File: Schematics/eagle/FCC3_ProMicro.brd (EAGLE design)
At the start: 42.9 x 36 mm, 9 parts, among them IC1 MCP3202P

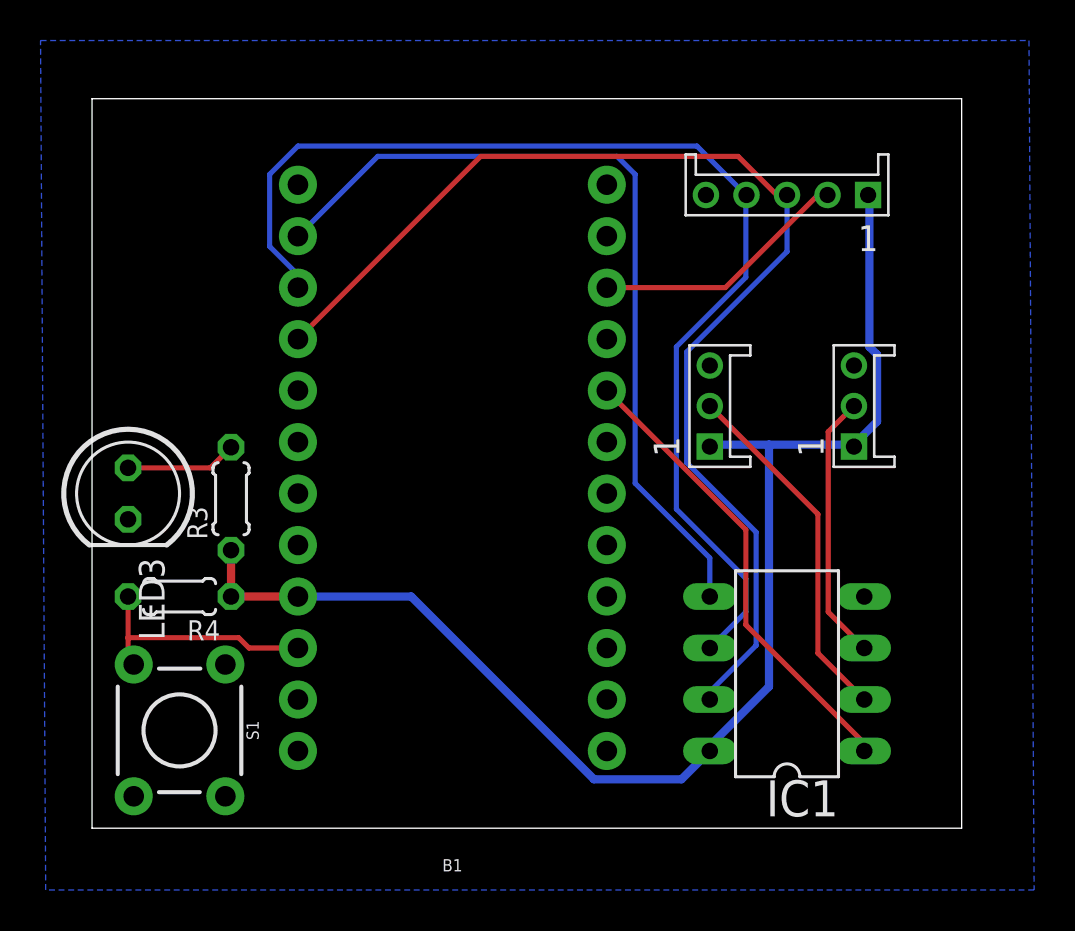
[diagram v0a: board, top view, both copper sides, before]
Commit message: replace force mapping with Analog/Digital FLCS
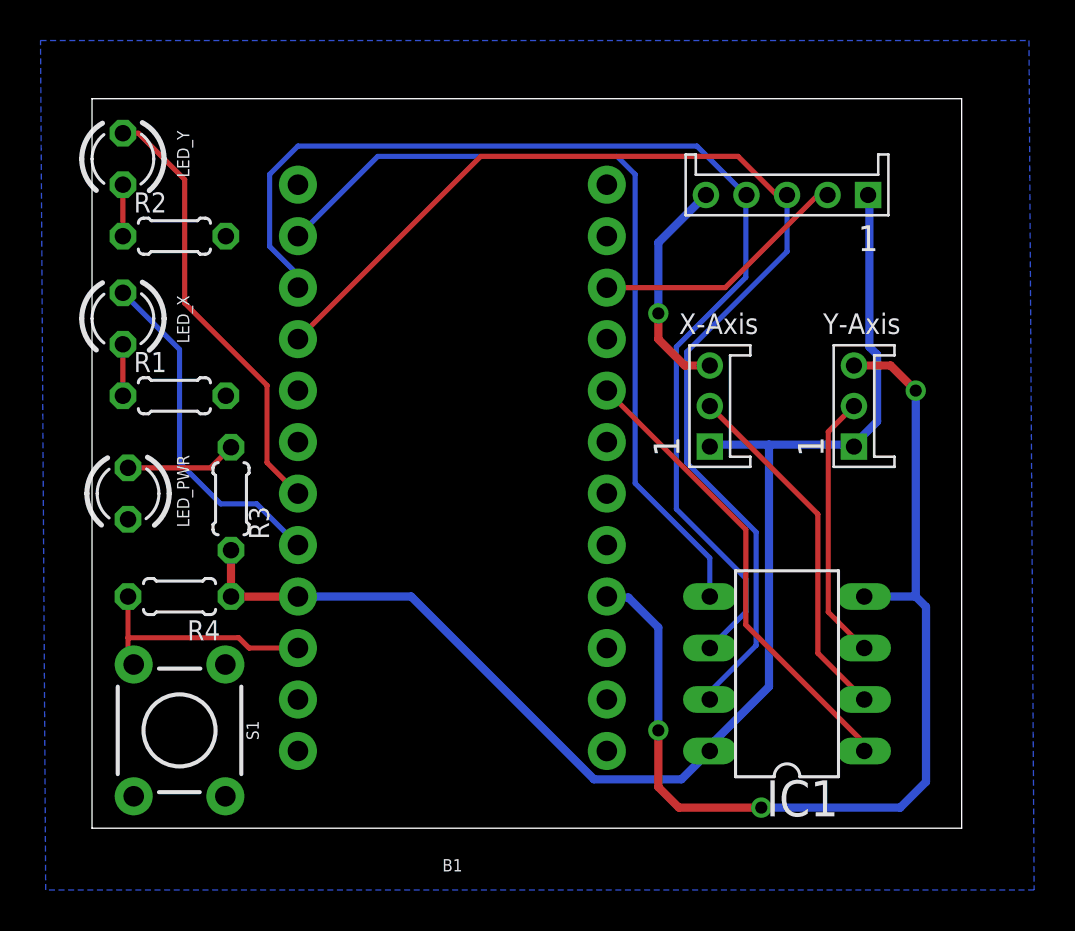
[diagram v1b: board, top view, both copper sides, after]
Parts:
- removed LED3: (no value), led:LED5MM
- added LED_PWR, LED_X, LED_Y: (no value), led:LED3MM
- added R1, R2: (no value), resistor:0204/5
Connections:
- new net N$3: B1.20, LED_X.A
- new net N$4: B1.19, LED_Y.A
- new net N$6: LED_Y.K, R2.1
- new net N$7: LED_X.K, R1.1
- net GND: now also LED_PWR.K, R1.2, R2.2; no longer LED3.K
- net N$5: now also LED_PWR.A; no longer LED3.A
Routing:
- net GND: track 0.00 -> 62.1 mm, vias 0 -> 4
- net N$4: track 0.00 -> 21.8 mm
- net N$3: track 0.00 -> 17.1 mm
- net N$7: track 0.00 -> 2.54 mm
- net N$6: track 0.00 -> 2.54 mm
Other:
- board text added: "X-Axis"
- board text added: "Y-Axis"
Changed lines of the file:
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@@
 <wire x1="42.906" y1="35.992" x2="0" y2="35.992" width="0" layer="20"/>
 <wire x1="0" y1="35.992" x2="0" y2="0" width="0" layer="20"/>
+<text x="28.956" y="24.384" size="1.016" layer="25">X-Axis</text>
+<text x="36.068" y="24.384" size="1.016" layer="25">Y-Axis</text>
 </plain>
 <attributes>
@@
 <attribute name="OC_FARNELL" value="1196794" x="34.29" y="7.62" size="1.778" layer="27" rot="R90" display="off"/>
 </element>
-<element name="LED3" library="led" package="LED5MM" value="" x="1.778" y="16.51" rot="R270"/>
-<element name="R3" library="resistor" package="0204/5" value="" x="6.858" y="16.256" rot="R90"/>
+<element name="LED_PWR" library="led" package="LED3MM" value="" x="1.778" y="16.51" smashed="yes" rot="R270">
+<attribute name="NAME" x="4.191" y="18.415" size="0.6096" layer="25" ratio="10" rot="R270"/>
+<attribute name="VALUE" x="0.127" y="14.605" size="1.27" layer="27" ratio="10" rot="R270"/>
+</element>
+<element name="R3" library="resistor" package="0204/5" value="" x="6.858" y="16.256" smashed="yes" rot="R90">
+<attribute name="NAME" x="8.7376" y="14.2494" size="0.9906" layer="25" ratio="10" rot="R90"/>
+<attribute name="VALUE" x="9.1694" y="14.1224" size="0.9906" layer="27" ratio="10" rot="R90"/>
+</element>
 <element name="R4" library="resistor" package="0204/5" value="" x="4.318" y="11.43" rot="R180"/>
 <element name="S1" library="SparkFun-Switches" package="TACTILE_SWITCH_PTH_6.0MM" value="MOMENTARY-SWITCH-SPST-PTH-6.0MM" x="4.318" y="4.826" rot="R270">
@@
 <element name="U$2" library="uriba" package="JST-EH-3PIN" value="JST_EH_3PIN" x="30.48" y="20.828" rot="R270"/>
 <element name="U$3" library="uriba" package="JST-EH-5PIN" value="JST_EH_5PIN" x="34.29" y="31.242"/>
+<element name="LED_X" library="led" package="LED3MM" value="" x="1.524" y="25.146" smashed="yes" rot="R270">
+<attribute name="NAME" x="4.191" y="26.289" size="0.6096" layer="25" ratio="10" rot="R270"/>
+<attribute name="VALUE" x="-0.127" y="23.241" size="1.27" layer="27" ratio="10" rot="R270"/>
+</element>
+<element name="LED_Y" library="led" package="LED3MM" value="" x="1.524" y="33.02" smashed="yes" rot="R270">
+<attribute name="NAME" x="4.191" y="34.417" size="0.6096" layer="25" ratio="10" rot="R270"/>
+<attribute name="VALUE" x="-0.127" y="31.115" size="1.27" layer="27" ratio="10" rot="R270"/>
+</element>
+<element name="R1" library="resistor" package="0204/5" value="" x="4.064" y="21.336"/>
+<element name="R2" library="resistor" package="0204/5" value="" x="4.064" y="29.21"/>
 </elements>
 <signals>
@@
 <contactref element="B1" pad="23"/>
 <contactref element="B1" pad="3"/>
-<contactref element="LED3" pad="K"/>
+<contactref element="LED_PWR" pad="K"/>
 <contactref element="S1" pad="1"/>
 <contactref element="B1" pad="4"/>
@@
 <vertex x="-2.286" y="-3.048"/>
 </polygon>
-<wire x1="37.592" y1="22.828" x2="38.1" y2="11.43" width="0" layer="19" extent="1-1"/>
-<wire x1="30.29" y1="31.242" x2="30.48" y2="22.828" width="0" layer="19" extent="1-1"/>
-<wire x1="25.4" y1="11.43" x2="30.48" y2="22.828" width="0" layer="19" extent="1-1"/>
+<contactref element="R1" pad="2"/>
+<contactref element="R2" pad="2"/>
+<wire x1="25.4" y1="9.017" x2="25.4" y2="8.89" width="0.4064" layer="16"/>
+<wire x1="37.592" y1="22.828" x2="39.402" y2="22.828" width="0.4064" layer="1"/>
+<wire x1="39.402" y1="22.828" x2="40.64" y2="21.59" width="0.4064" layer="1"/>
+<via x="40.64" y="21.59" extent="1-16" drill="0.6" shape="square"/>
+<wire x1="40.64" y1="21.59" x2="40.64" y2="11.43" width="0.4064" layer="16"/>
+<wire x1="40.64" y1="11.43" x2="38.1" y2="11.43" width="0.4064" layer="16"/>
+<wire x1="30.48" y1="22.828" x2="29.242" y2="22.828" width="0.4064" layer="1"/>
+<wire x1="29.242" y1="22.828" x2="27.94" y2="24.13" width="0.4064" layer="1"/>
+<wire x1="27.94" y1="24.13" x2="27.94" y2="25.4" width="0.4064" layer="1"/>
+<via x="27.94" y="25.4" extent="1-16" drill="0.6" shape="square"/>
+<wire x1="27.94" y1="25.4" x2="27.94" y2="28.892" width="0.4064" layer="16"/>
+<wire x1="27.94" y1="28.892" x2="30.29" y2="31.242" width="0.4064" layer="16"/>
+<wire x1="25.34919375" y1="11.379178125" x2="26.466821875" y2="11.379178125" width="0.4064" layer="16"/>
+<wire x1="26.466821875" y1="11.379178125" x2="27.94" y2="9.906" width="0.4064" layer="16"/>
+<wire x1="27.94" y1="9.906" x2="27.94" y2="4.826" width="0.4064" layer="16"/>
+<via x="27.94" y="4.826" extent="1-16" drill="0.6" shape="square"/>
+<wire x1="27.94" y1="4.826" x2="27.94" y2="2.032" width="0.4064" layer="1"/>
+<wire x1="27.94" y1="2.032" x2="28.956" y2="1.016" width="0.4064" layer="1"/>
+<wire x1="28.956" y1="1.016" x2="33.02" y2="1.016" width="0.4064" layer="1"/>
+<via x="33.02" y="1.016" extent="1-16" drill="0.6" shape="square"/>
+<wire x1="33.02" y1="1.016" x2="39.878" y2="1.016" width="0.4064" layer="16"/>
+<wire x1="39.878" y1="1.016" x2="41.148" y2="2.286" width="0.4064" layer="16"/>
+<wire x1="41.148" y1="2.286" x2="41.148" y2="10.922" width="0.4064" layer="16"/>
+<wire x1="41.148" y1="10.922" x2="40.64" y2="11.43" width="0.4064" layer="16"/>
 </signal>
 <signal name="RAW">
@@
 </signal>
 <signal name="N$5">
-<contactref element="LED3" pad="A"/>
+<contactref element="LED_PWR" pad="A"/>
 <contactref element="R3" pad="2"/>
 <wire x1="5.842" y1="17.78" x2="1.778" y2="17.78" width="0.254" layer="1"/>
@@
 <wire x1="38.1" y1="8.89" x2="36.322" y2="10.668" width="0.254" layer="1"/>
 </signal>
+<signal name="N$3">
+<contactref element="B1" pad="20"/>
+<contactref element="LED_X" pad="A"/>
+<wire x1="10.16" y1="13.97" x2="8.128" y2="16.002" width="0.254" layer="16"/>
+<wire x1="8.128" y1="16.002" x2="6.35" y2="16.002" width="0.254" layer="16"/>
+<wire x1="6.35" y1="16.002" x2="4.318" y2="18.034" width="0.254" layer="16"/>
+<wire x1="4.318" y1="18.034" x2="4.318" y2="23.622" width="0.254" layer="16"/>
+<wire x1="4.318" y1="23.622" x2="1.524" y2="26.416" width="0.254" layer="16"/>
+</signal>
+<signal name="N$4">
+<contactref element="B1" pad="19"/>
+<contactref element="LED_Y" pad="A"/>
+<wire x1="10.16" y1="16.51" x2="8.636" y2="18.034" width="0.254" layer="1"/>
+<wire x1="8.636" y1="18.034" x2="8.636" y2="21.844" width="0.254" layer="1"/>
+<wire x1="8.636" y1="21.844" x2="4.572" y2="25.908" width="0.254" layer="1"/>
+<wire x1="4.572" y1="25.908" x2="4.572" y2="32.004" width="0.254" layer="1"/>
+<wire x1="4.572" y1="32.004" x2="2.286" y2="34.29" width="0.254" layer="1"/>
+<wire x1="2.286" y1="34.29" x2="1.524" y2="34.29" width="0.254" layer="1"/>
+</signal>
+<signal name="N$6">
+<contactref element="LED_Y" pad="K"/>
+<contactref element="R2" pad="1"/>
+<wire x1="1.524" y1="29.21" x2="1.524" y2="31.75" width="0.254" layer="1"/>
+</signal>
+<signal name="N$7">
+<contactref element="LED_X" pad="K"/>
+<contactref element="R1" pad="1"/>
+<wire x1="1.524" y1="21.336" x2="1.524" y2="23.876" width="0.254" layer="1"/>
+</signal>
 </signals>
